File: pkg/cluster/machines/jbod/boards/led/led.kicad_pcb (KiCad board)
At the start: 2 copper layers, 138.5 x 6 mm, 7 parts, among them J1 OUT, J2 IN, U1 WS2812B-2020, U2 WS2812B-2020, U3 WS2812B-2020, U4 WS2812B-2020, U5 WS2812B-2020

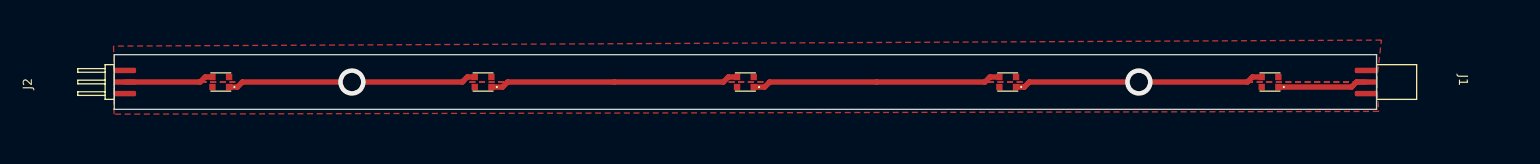
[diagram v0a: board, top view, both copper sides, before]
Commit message: Add cluster blob replication and separate resolver service.
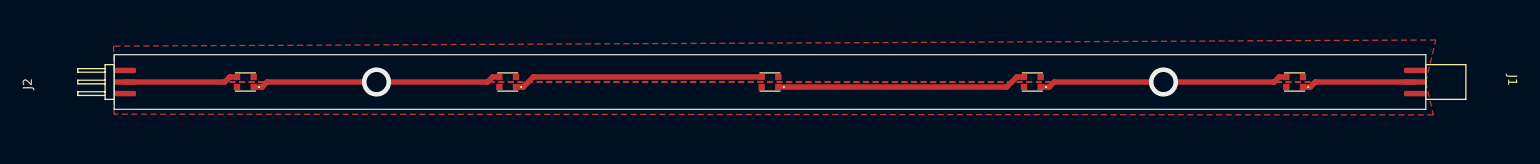
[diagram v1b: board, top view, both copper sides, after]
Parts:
- moved J1 5.40 mm to (243.9, 103.0)
- moved U5 2.70 mm to (229.5, 103.0)
- moved U4 2.70 mm to (200.8, 103.0)
- moved U3 2.70 mm to (172.0, 103.0)
- moved U2 2.70 mm to (143.2, 103.0)
- moved U1 2.70 mm to (114.4, 103.0)
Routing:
- net Net-(J2-Pin_2): track 9.80 -> 12.5 mm
- net Net-(J1-Pin_2): track 9.80 -> 12.5 mm
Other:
- board size 138.5 x 6 mm -> 143.9 x 6 mm
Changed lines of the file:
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@@
   (net 8 "Net-(J2-Pin_2)")
   (footprint "Components:PinReceptacle_Edge_1.27mm_3P" (layer "F.Cu")
-    (at 238.53 103 -90)
+    (at 243.93 103 -90)
     (property "Sheetfile" "led.kicad_sch")
     (property "Sheetname" "")
@@
   )
   (footprint "Components:WS2812B-2020" (layer "F.Cu")
-    (at 140.478333 103)
+    (at 143.178 103)
     (property "Sheetfile" "led.kicad_sch")
     (property "Sheetname" "")
@@
   )
   (footprint "Components:WS2812B-2020" (layer "F.Cu")
-    (at 226.838333 103)
+    (at 229.539 103)
     (property "Sheetfile" "led.kicad_sch")
     (property "Sheetname" "")
@@
   )
   (footprint "Components:WS2812B-2020" (layer "F.Cu")
-    (at 169.265 103)
+    (at 171.965 103)
     (property "Sheetfile" "led.kicad_sch")
     (property "Sheetname" "")
@@
   )
   (footprint "Components:WS2812B-2020" (layer "F.Cu")
-    (at 198.051667 103)
+    (at 200.752 103)
     (property "Sheetfile" "led.kicad_sch")
     (property "Sheetname" "")
@@
   )
   (footprint "Components:WS2812B-2020" (layer "F.Cu")
-    (at 111.691667 103)
+    (at 114.391 103)
     (property "Sheetfile" "led.kicad_sch")
     (property "Sheetname" "")
@@
       (net 1 "+5V") (pinfunction "VDD") (pintype "input"))
   )
-  (gr_line (start 238.53 106) (end 238.53 100)
-    (stroke (width 0.1) (type default)) (layer "Edge.Cuts"))
-  (gr_line (start 100 106) (end 238.53 106)
+  (gr_line (start 243.93 106) (end 243.93 100)
+    (stroke (width 0.1) (type default)) (layer "Edge.Cuts"))
+  (gr_line (start 100 106) (end 243.93 106)
     (stroke (width 0.1) (type default)) (layer "Edge.Cuts"))
   (gr_line (start 100 100) (end 100 106)
     (stroke (width 0.1) (type default)) (layer "Edge.Cuts"))
-  (gr_line (start 100 100) (end 238.53 100)
-    (stroke (width 0.1) (type default)) (layer "Edge.Cuts"))
-  (segment (start 114.0684 103) (end 113.5184 103.55) (width 0.6) (layer "F.Cu") (net 3))
-  (segment (start 126.085 103) (end 114.0684 103) (width 0.6) (layer "F.Cu") (net 3))
-  (segment (start 138.1984 103) (end 138.7484 102.45) (width 0.6) (layer "F.Cu") (net 3))
-  (segment (start 113.5184 103.55) (end 112.606667 103.55) (width 0.6) (layer "F.Cu") (net 3))
-  (segment (start 138.7484 102.45) (end 139.563333 102.45) (width 0.6) (layer "F.Cu") (net 3))
-  (segment (start 126.085 103) (end 138.1984 103) (width 0.6) (layer "F.Cu") (net 3))
-  (via (at 126.085 103) (size 3) (drill 2) (layers "F.Cu" "B.Cu") (net 3))
-  (segment (start 166.8496 103) (end 167.3996 102.45) (width 0.6) (layer "F.Cu") (net 4))
-  (segment (start 142.6268 103.55) (end 141.393333 103.55) (width 0.6) (layer "F.Cu") (net 4))
-  (segment (start 154.871667 103) (end 166.8496 103) (width 0.6) (layer "F.Cu") (net 4))
-  (segment (start 143.1768 103) (end 142.6268 103.55) (width 0.6) (layer "F.Cu") (net 4))
-  (segment (start 167.3996 102.45) (end 168.35 102.45) (width 0.6) (layer "F.Cu") (net 4))
-  (segment (start 154.871667 103) (end 143.1768 103) (width 0.6) (layer "F.Cu") (net 4))
-  (segment (start 195.5516 103) (end 196.1016 102.45) (width 0.6) (layer "F.Cu") (net 5))
-  (segment (start 183.658334 103) (end 195.5516 103) (width 0.6) (layer "F.Cu") (net 5))
-  (segment (start 171.9296 103) (end 171.3796 103.55) (width 0.6) (layer "F.Cu") (net 5))
-  (segment (start 196.1016 102.45) (end 197.136667 102.45) (width 0.6) (layer "F.Cu") (net 5))
-  (segment (start 171.3796 103.55) (end 170.18 103.55) (width 0.6) (layer "F.Cu") (net 5))
-  (segment (start 183.658334 103) (end 171.9296 103) (width 0.6) (layer "F.Cu") (net 5))
-  (segment (start 224.3552 103) (end 224.9052 102.45) (width 0.6) (layer "F.Cu") (net 6))
-  (segment (start 224.9052 102.45) (end 225.923333 102.45) (width 0.6) (layer "F.Cu") (net 6))
-  (segment (start 212.445001 103) (end 224.3552 103) (width 0.6) (layer "F.Cu") (net 6))
-  (segment (start 200.4284 103) (end 199.8784 103.55) (width 0.6) (layer "F.Cu") (net 6))
-  (segment (start 212.445001 103) (end 200.4284 103) (width 0.6) (layer "F.Cu") (net 6))
-  (segment (start 199.8784 103.55) (end 198.966667 103.55) (width 0.6) (layer "F.Cu") (net 6))
-  (via (at 212.445001 103) (size 3) (drill 2) (layers "F.Cu" "B.Cu") (net 6))
-  (segment (start 235.785184 103.55) (end 236.335184 103) (width 0.6) (layer "F.Cu") (net 7))
-  (segment (start 236.335184 103) (end 237.33 103) (width 0.6) (layer "F.Cu") (net 7))
-  (segment (start 227.753333 103.55) (end 235.785184 103.55) (width 0.6) (layer "F.Cu") (net 7))
-  (segment (start 109.976667 102.45) (end 110.776667 102.45) (width 0.6) (layer "F.Cu") (net 8))
-  (segment (start 109.426667 103) (end 109.976667 102.45) (width 0.6) (layer "F.Cu") (net 8))
-  (segment (start 101.2 103) (end 109.426667 103) (width 0.6) (layer "F.Cu") (net 8))
+  (gr_line (start 100 100) (end 243.93 100)
+    (stroke (width 0.1) (type default)) (layer "Edge.Cuts"))
+  (segment (start 140.97 103) (end 141.52 102.45) (width 0.6) (layer "F.Cu") (net 3))
+  (segment (start 141.52 102.45) (end 142.263 102.45) (width 0.6) (layer "F.Cu") (net 3))
+  (segment (start 116.23 103.55) (end 115.306 103.55) (width 0.6) (layer "F.Cu") (net 3))
+  (segment (start 128.7845 103) (end 140.97 103) (width 0.6) (layer "F.Cu") (net 3))
+  (segment (start 116.78 103) (end 116.23 103.55) (width 0.6) (layer "F.Cu") (net 3))
+  (segment (start 128.7845 103) (end 116.78 103) (width 0.6) (layer "F.Cu") (net 3))
+  (via (at 128.7845 103) (size 3.2) (drill 2.2) (layers "F.Cu" "B.Cu") (net 3))
+  (segment (start 144.893 103.55) (end 144.093 103.55) (width 0.6) (layer "F.Cu") (net 4))
+  (segment (start 145.993 102.45) (end 144.893 103.55) (width 0.6) (layer "F.Cu") (net 4))
+  (segment (start 171.05 102.45) (end 145.993 102.45) (width 0.6) (layer "F.Cu") (net 4))
+  (segment (start 197.937 103.55) (end 199.037 102.45) (width 0.6) (layer "F.Cu") (net 5))
+  (segment (start 172.88 103.55) (end 197.937 103.55) (width 0.6) (layer "F.Cu") (net 5))
+  (segment (start 199.037 102.45) (end 199.837 102.45) (width 0.6) (layer "F.Cu") (net 5))
+  (segment (start 227.84 102.45) (end 228.624 102.45) (width 0.6) (layer "F.Cu") (net 6))
+  (segment (start 215.1455 103) (end 203.15 103) (width 0.6) (layer "F.Cu") (net 6))
+  (segment (start 227.29 103) (end 227.84 102.45) (width 0.6) (layer "F.Cu") (net 6))
+  (segment (start 203.15 103) (end 202.6 103.55) (width 0.6) (layer "F.Cu") (net 6))
+  (segment (start 215.1455 103) (end 227.29 103) (width 0.6) (layer "F.Cu") (net 6))
+  (segment (start 202.6 103.55) (end 201.667 103.55) (width 0.6) (layer "F.Cu") (net 6))
+  (via (at 215.1455 103) (size 3.2) (drill 2.2) (layers "F.Cu" "B.Cu") (net 6))
+  (segment (start 231.254 103.55) (end 230.454 103.55) (width 0.6) (layer "F.Cu") (net 7))
+  (segment (start 242.73 103) (end 231.804 103) (width 0.6) (layer "F.Cu") (net 7))
+  (segment (start 231.804 103) (end 231.254 103.55) (width 0.6) (layer "F.Cu") (net 7))
+  (segment (start 101.2 103) (end 112.126 103) (width 0.6) (layer "F.Cu") (net 8))
+  (segment (start 112.676 102.45) (end 113.476 102.45) (width 0.6) (layer "F.Cu") (net 8))
+  (segment (start 112.126 103) (end 112.676 102.45) (width 0.6) (layer "F.Cu") (net 8))
   (zone (net 2) (net_name "GND") (layer "F.Cu") (hatch edge 0.5)
     (priority 1)
@@
       (pts
         (xy 100 103)
-        (xy 238.53 103)
-        (xy 239.0648 98.3996)
+        (xy 243.93 103)
+        (xy 245.03 98.39)
         (xy 99.9236 99.06)
       )
@@
       (pts
         (xy 100 103)
-        (xy 238.53 103)
-        (xy 238.76 106.2228)
+        (xy 243.93 103)
+        (xy 244.76 106.61)
         (xy 99.9744 106.5276)
       )

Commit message: Flushing some recent changes.
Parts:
- moved J1 1.00 mm to (242.9, 103.0)
- moved J2 1.00 mm to (101.0, 103.0)
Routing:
- net Net-(J2-Pin_2): track 12.5 -> 11.5 mm
- net Net-(J1-Pin_2): track 12.5 -> 11.5 mm
- added copper zone on B.Cu, net GND
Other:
- board size 143.9 x 6 mm -> 141.9 x 6 mm
- board text added: "+"
- board text added: "-"
- board text added: "Note: Bottom side is unused and is only filled to increase the rigidity of the PCB."
- board text added: "in"
- board text added: "out"
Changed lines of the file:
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@@
   (net 8 "Net-(J2-Pin_2)")
   (footprint "Components:PinReceptacle_Edge_1.27mm_3P" (layer "F.Cu")
-    (at 243.93 103 -90)
+    (at 242.93 103 -90)
     (property "Sheetfile" "led.kicad_sch")
     (property "Sheetname" "")
@@
   )
   (footprint "Components:PinHeader_Edge_1.27mm_3P" (layer "F.Cu")
-    (at 100 103 90)
+    (at 101 103 90)
     (property "Sheetfile" "led.kicad_sch")
     (property "Sheetname" "")
@@
   )
   (gr_line (start 243.93 106) (end 243.93 100)
+    (stroke (width 0.1) (type default)) (layer "Cmts.User"))
+  (gr_line (start 100 100) (end 100 106)
+    (stroke (width 0.1) (type default)) (layer "Cmts.User"))
+  (gr_line (start 242.93 106) (end 242.93 100)
     (stroke (width 0.1) (type default)) (layer "Edge.Cuts"))
-  (gr_line (start 100 106) (end 243.93 106)
+  (gr_line (start 101 106) (end 242.93 106)
     (stroke (width 0.1) (type default)) (layer "Edge.Cuts"))
-  (gr_line (start 100 100) (end 100 106)
+  (gr_line (start 101 100) (end 101 106)
     (stroke (width 0.1) (type default)) (layer "Edge.Cuts"))
-  (gr_line (start 100 100) (end 243.93 100)
+  (gr_line (start 101 100) (end 242.93 100)
     (stroke (width 0.1) (type default)) (layer "Edge.Cuts"))
+  (gr_text "in" (at 103.7 103.6) (layer "F.SilkS")
+    (effects (font (size 1 1) (thickness 0.15)) (justify left bottom))
+  )
+  (gr_text "-" (at 103.7 102.25) (layer "F.SilkS")
+    (effects (font (size 1 1) (thickness 0.15)) (justify left bottom))
+  )
+  (gr_text "out" (at 237.6 103.5) (layer "F.SilkS")
+    (effects (font (size 1 1) (thickness 0.15)) (justify left bottom))
+  )
+  (gr_text "+" (at 238.7 104.8) (layer "F.SilkS")
+    (effects (font (size 1 1) (thickness 0.15)) (justify left bottom))
+  )
+  (gr_text "+" (at 103.7 104.85) (layer "F.SilkS")
+    (effects (font (size 1 1) (thickness 0.15)) (justify left bottom))
+  )
+  (gr_text "-" (at 238.7 102.2) (layer "F.SilkS")
+    (effects (font (size 1 1) (thickness 0.15)) (justify left bottom))
+  )
+  (gr_text "Note: Bottom side is unused and is only filled to increase the rigidity of the PCB." (at 99.25 98.25) (layer "User.1")
+    (effects (font (size 1 1) (thickness 0.15)) (justify left bottom))
+  )
   (segment (start 140.97 103) (end 141.52 102.45) (width 0.6) (layer "F.Cu") (net 3))
   (segment (start 141.52 102.45) (end 142.263 102.45) (width 0.6) (layer "F.Cu") (net 3))
@@
   (via (at 215.1455 103) (size 3.2) (drill 2.2) (layers "F.Cu" "B.Cu") (net 6))
   (segment (start 231.254 103.55) (end 230.454 103.55) (width 0.6) (layer "F.Cu") (net 7))
-  (segment (start 242.73 103) (end 231.804 103) (width 0.6) (layer "F.Cu") (net 7))
   (segment (start 231.804 103) (end 231.254 103.55) (width 0.6) (layer "F.Cu") (net 7))
-  (segment (start 101.2 103) (end 112.126 103) (width 0.6) (layer "F.Cu") (net 8))
+  (segment (start 241.73 103) (end 231.804 103) (width 0.6) (layer "F.Cu") (net 7))
+  (segment (start 112.126 103) (end 112.676 102.45) (width 0.6) (layer "F.Cu") (net 8))
+  (segment (start 102.2 103) (end 112.126 103) (width 0.6) (layer "F.Cu") (net 8))
   (segment (start 112.676 102.45) (end 113.476 102.45) (width 0.6) (layer "F.Cu") (net 8))
-  (segment (start 112.126 103) (end 112.676 102.45) (width 0.6) (layer "F.Cu") (net 8))
   (zone (net 2) (net_name "GND") (layer "F.Cu") (hatch edge 0.5)
     (priority 1)
@@
       )
     )
+  )
+  (zone (net 2) (net_name "GND") (layer "B.Cu") (hatch edge 0.5)
+    (priority 2)
+    (connect_pads (clearance 0.5))
+    (min_thickness 0.25) (filled_areas_thickness no)
+    (fill yes (thermal_gap 0.5) (thermal_bridge_width 0.5))
+    (polygon
+      (pts
+        (xy 97.5 96)
+        (xy 246.75 97)
+        (xy 246.75 108)
+        (xy 89.5 110)
+        (xy 90.5 96.5)
+      )
+    )
